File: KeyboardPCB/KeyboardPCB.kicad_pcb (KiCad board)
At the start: 2 copper layers, 88.9 x 86.4 mm, 178 parts, among them P1 USB_C_Plug, P2 USB_C_Plug, Q1 CSD17527Q5A, Q2 CSD17527Q5A, U1 ATmega32U4-M, U2 TPS61236PRWLT, U3 BQ24193RGER, U4 BQ297xy, Y1 ECS-160-7-33B-CKL-TR

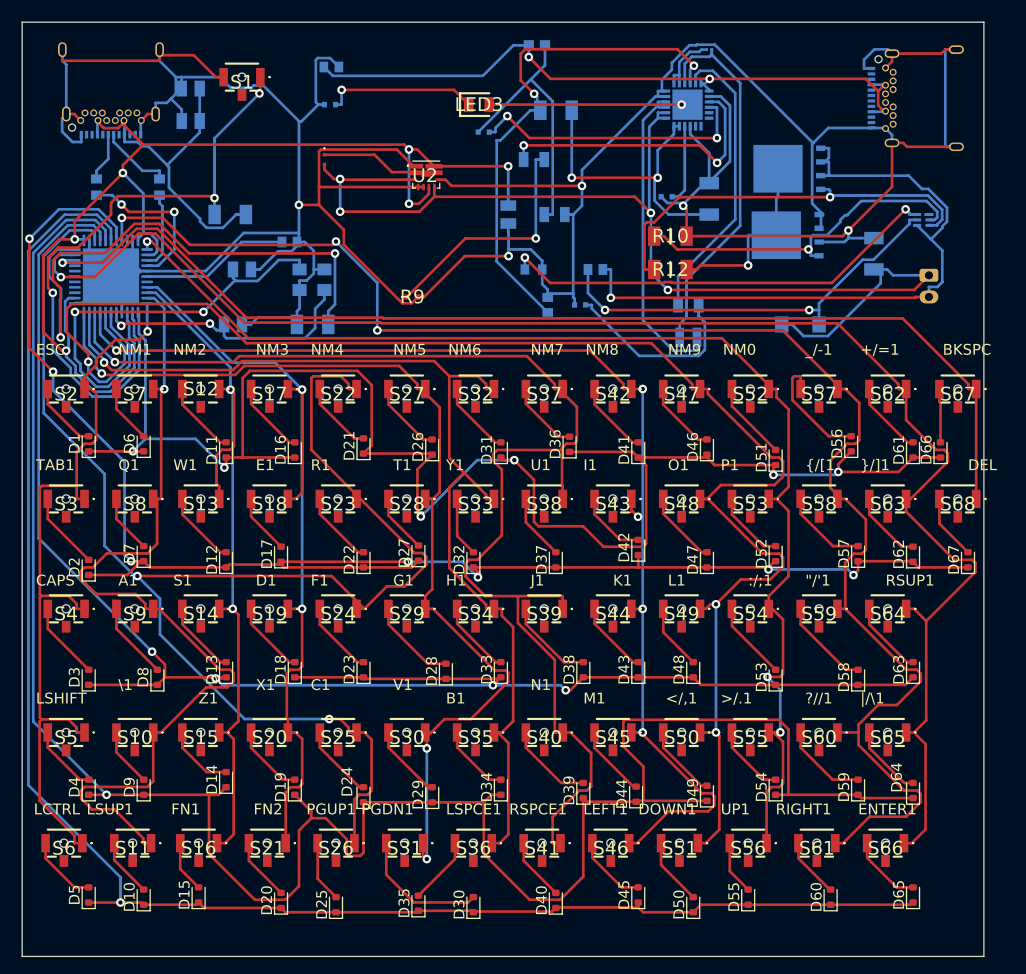
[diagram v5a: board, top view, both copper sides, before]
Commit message: Added switch and modified pcb to account for it
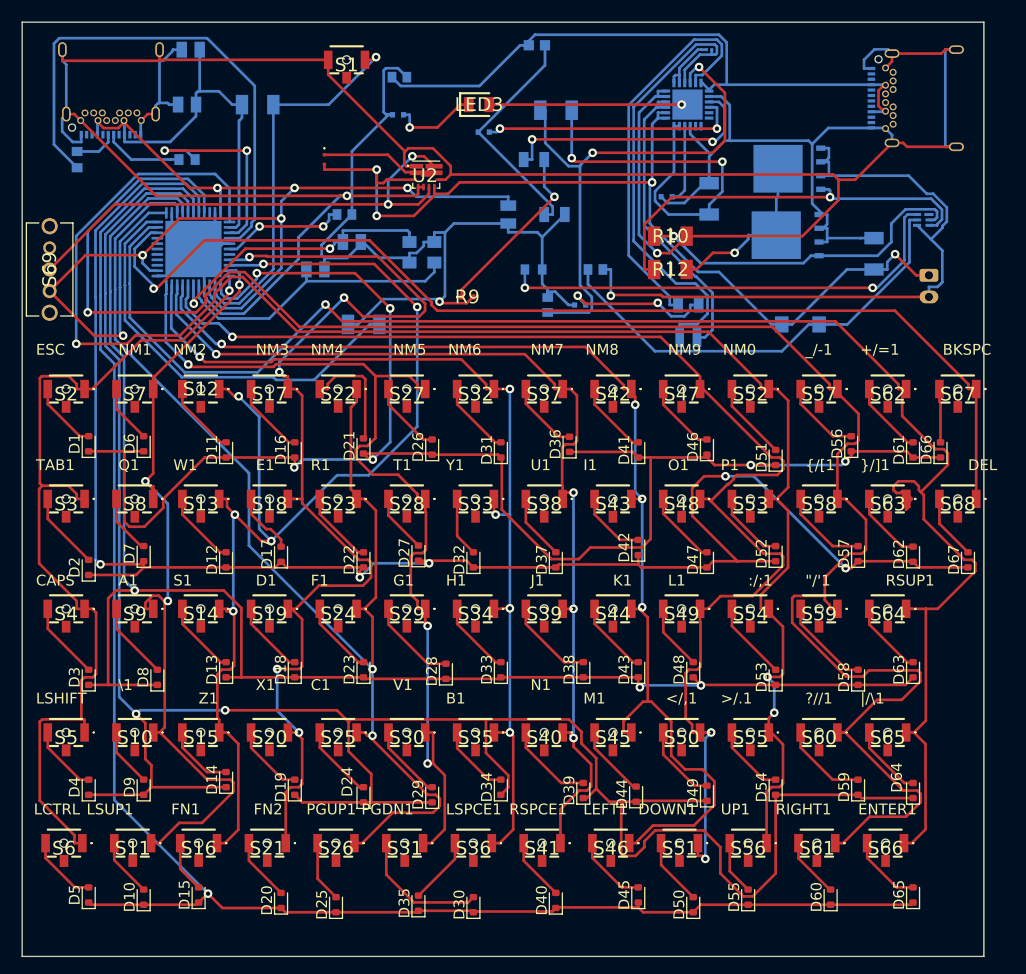
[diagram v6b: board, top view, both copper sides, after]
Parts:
- added S69: 1825232-1, keyboard_syms:18252321, F.Cu at (61.0, 47.7)
- moved C2 10.5 mm to (88.9, 43.2)
- moved Y1 10.5 mm to (95.4, 44.1)
- moved R3 10.5 mm to (80.2, 30.5), turned to 0 degrees
- moved S1 9.80 mm to (88.4, 26.3)
- moved C3 9.16 mm to (85.5, 45.7)
- moved U1 8.03 mm to (74.2, 43.8)
- moved C1 6.36 mm to (93.3, 27.9)
- moved R8 6.36 mm to (93.2, 31.4)
- moved C4 5.68 mm to (88.2, 40.6)
- moved R9 5.08 mm to (99.6, 48.3)
- moved R4 4.72 mm to (90.0, 50.8)
- moved C5 3.60 mm to (74.0, 25.4)
- moved R2 3.59 mm to (73.7, 35.6), turned to 0 degrees
- moved R1 3.11 mm to (63.5, 35.6)
- moved C7 1.56 mm to (73.7, 30.5)
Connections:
- U2 pad 6: /MCU_Battery/VBUSOUT -> Net-(U2-FB)
- U2 pad 9: /MCU_Battery/VBUSOUT -> Net-(U2-FB)
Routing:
- net Net-(U2-FB): track 0.00 -> 46.3 mm, vias 0 -> 2
- net /Key_Array/ICOL10: track 114.9 -> 152.4 mm
- net /Key_Array/ICOL2: track 71.1 -> 107.2 mm, vias 2 -> 6
- net Net-(U1-D+): track 14.4 -> 48.6 mm, vias 2 -> 0
- net GND: track 359.6 -> 392.3 mm, vias 5 -> 3
- net /Key_Array/ICOL11: track 144.2 -> 175.4 mm, vias 3 -> 1
- net /Key_Array/ICOL7: track 120.4 -> 91.8 mm, vias 1 -> 4
- net /Key_Array/ICOL4: track 138.4 -> 113.2 mm
- net Net-(S1-C1): track 58.3 -> 35.5 mm, vias 3 -> 1
- net /Key_Array/ICOL3: track 77.0 -> 99.8 mm, vias 2 -> 5
- net /Key_Array/ICOL9: track 143.7 -> 121.4 mm
- net +BATT: track 104.7 -> 87.4 mm
- net Net-(U1-XTAL1): track 42.0 -> 26.4 mm
- net Net-(U1-~{HWB}/PE2): track 53.4 -> 38.8 mm, vias 2 -> 0
- net Net-(U1-D-): track 7.20 -> 19.5 mm, vias 0 -> 2
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
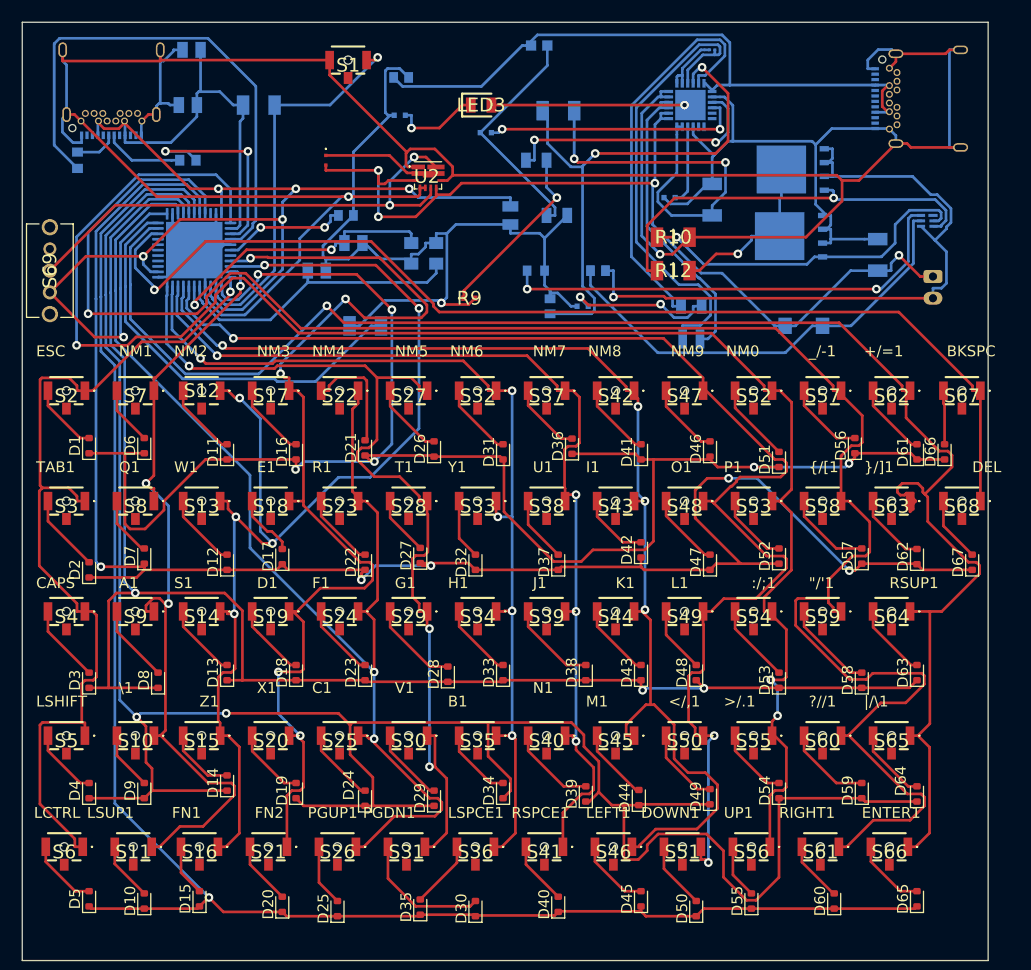
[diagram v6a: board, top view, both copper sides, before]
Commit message: Changed location of switch
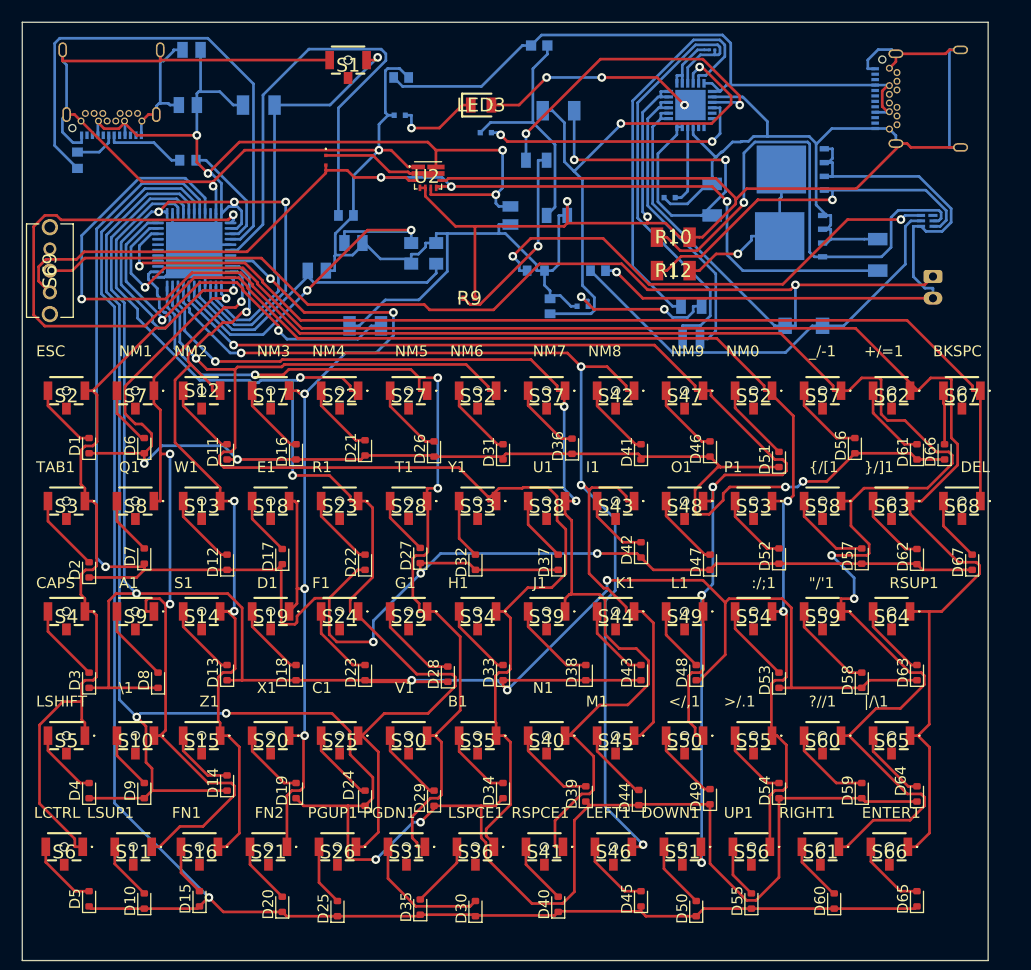
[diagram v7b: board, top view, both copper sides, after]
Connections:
- L1 pad 2: +BATT -> Net-(U2-EN)
- R5 pad 2: +BATT -> Net-(U2-EN)
- S69 pad 1: /MCU_Battery/VBUSOUT -> Net-(U2-EN)
- S69 pad 2: Net-(U2-FB) -> +BATT
- U2 pad 3: +BATT -> Net-(U2-EN)
- U2 pad 6: Net-(U2-FB) -> /MCU_Battery/VBUSOUT
- U2 pad 7: +BATT -> Net-(U2-EN)
- U2 pad 9: Net-(U2-FB) -> /MCU_Battery/VBUSOUT
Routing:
- net Net-(U2-EN): track 0.00 -> 95.8 mm, vias 0 -> 3
- net Net-(U2-FB): track 46.3 -> 0.00 mm, vias 2 -> 0
- net /Key_Array/IROW2: track 142.8 -> 185.6 mm, vias 3 -> 4
- net /Key_Array/ICOL2: track 107.2 -> 71.0 mm, vias 6 -> 3
- net Net-(U1-UCAP): track 11.6 -> 45.8 mm, vias 2 -> 0
- net /Key_Array/ICOL6: track 87.3 -> 121.4 mm, vias 5 -> 1
- net /Key_Array/IROW0: track 154.1 -> 120.9 mm, vias 6 -> 5
- net +BATT: track 87.4 -> 118.7 mm, vias 4 -> 1
- net /Key_Array/ICOL8: track 106.3 -> 128.1 mm
- net GND: track 392.3 -> 374.7 mm, vias 3 -> 4
- net Net-(Q1-G): track 31.7 -> 48.6 mm
- net /Key_Array/ICOL3: track 99.8 -> 87.0 mm
- net /Key_Array/ICOL7: track 91.8 -> 101.9 mm, vias 4 -> 3
- net /MCU_Battery/VBUSOUT: track 145.5 -> 135.5 mm, vias 6 -> 7
- net /Key_Array/ICOL4: track 113.2 -> 103.9 mm
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
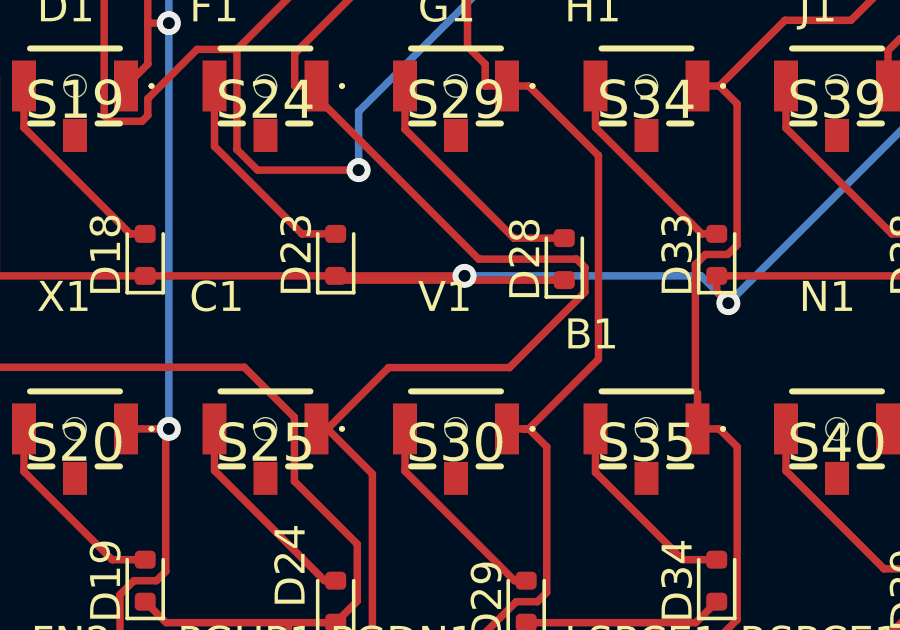
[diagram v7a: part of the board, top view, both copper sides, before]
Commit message: Small modification to tracks
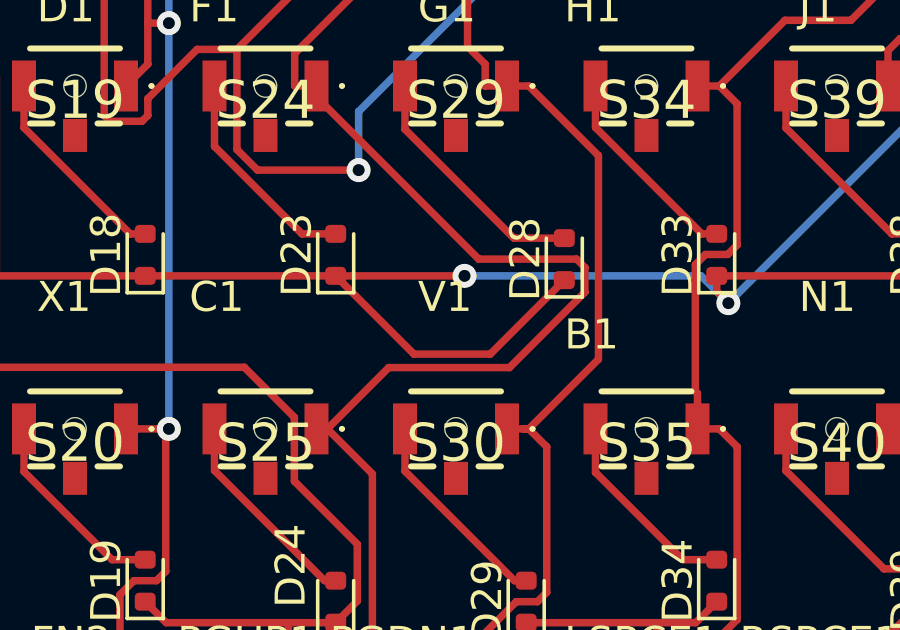
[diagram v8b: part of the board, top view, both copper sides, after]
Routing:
- net /Key_Array/IROW2: track 185.6 -> 187.7 mm
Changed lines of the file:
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@@
   (segment (start 64.57 92.88) (end 63.7571 92.88) (width 0.25) (layer "F.Cu") (net 16))
   (segment (start 68.9384 75.4429) (end 67.0615 75.4429) (width 0.25) (layer "F.Cu") (net 17))
+  (segment (start 97.59 83.5612) (end 95.1236 86.0276) (width 0.25) (layer "F.Cu") (net 17))
   (segment (start 102.67 83.9403) (end 103.0581 84.3284) (width 0.25) (layer "F.Cu") (net 17))
+  (segment (start 95.1236 86.0276) (end 92.5776 86.0276) (width 0.25) (layer "F.Cu") (net 17))
   (segment (start 66.3755 84.12) (end 70.92 84.12) (width 0.25) (layer "F.Cu") (net 17))
   (segment (start 115.37 83.42) (end 110.29 83.42) (width 0.25) (layer "F.Cu") (net 17))
@@
   (segment (start 66.3755 76.1289) (end 66.3755 84.12) (width 0.25) (layer "F.Cu") (net 17))
   (segment (start 102.67 83.42) (end 102.67 83.9403) (width 0.25) (layer "F.Cu") (net 17))
-  (segment (start 97.59 83.5612) (end 90.1112 83.5612) (width 0.25) (layer "F.Cu") (net 17))
   (segment (start 123.4768 75.9131) (end 123.1221 76.2678) (width 0.25) (layer "F.Cu") (net 17))
   (segment (start 120.45 83.42) (end 120.7798 83.42) (width 0.25) (layer "F.Cu") (net 17))
@@
   (segment (start 121.0744 74.2201) (end 112.2445 74.2201) (width 0.25) (layer "F.Cu") (net 17))
   (segment (start 110.29 83.42) (end 102.67 83.42) (width 0.25) (layer "F.Cu") (net 17))
-  (segment (start 90.1112 83.5612) (end 89.97 83.42) (width 0.25) (layer "F.Cu") (net 17))
+  (segment (start 92.5776 86.0276) (end 89.97 83.42) (width 0.25) (layer "F.Cu") (net 17))
   (segment (start 78.659 83.42) (end 77.27 83.42) (width 0.25) (layer "F.Cu") (net 17))
   (segment (start 83.62 83.42) (end 89.97 83.42) (width 0.25) (layer "F.Cu") (net 17))
